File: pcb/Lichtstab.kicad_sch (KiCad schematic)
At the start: 0 parts

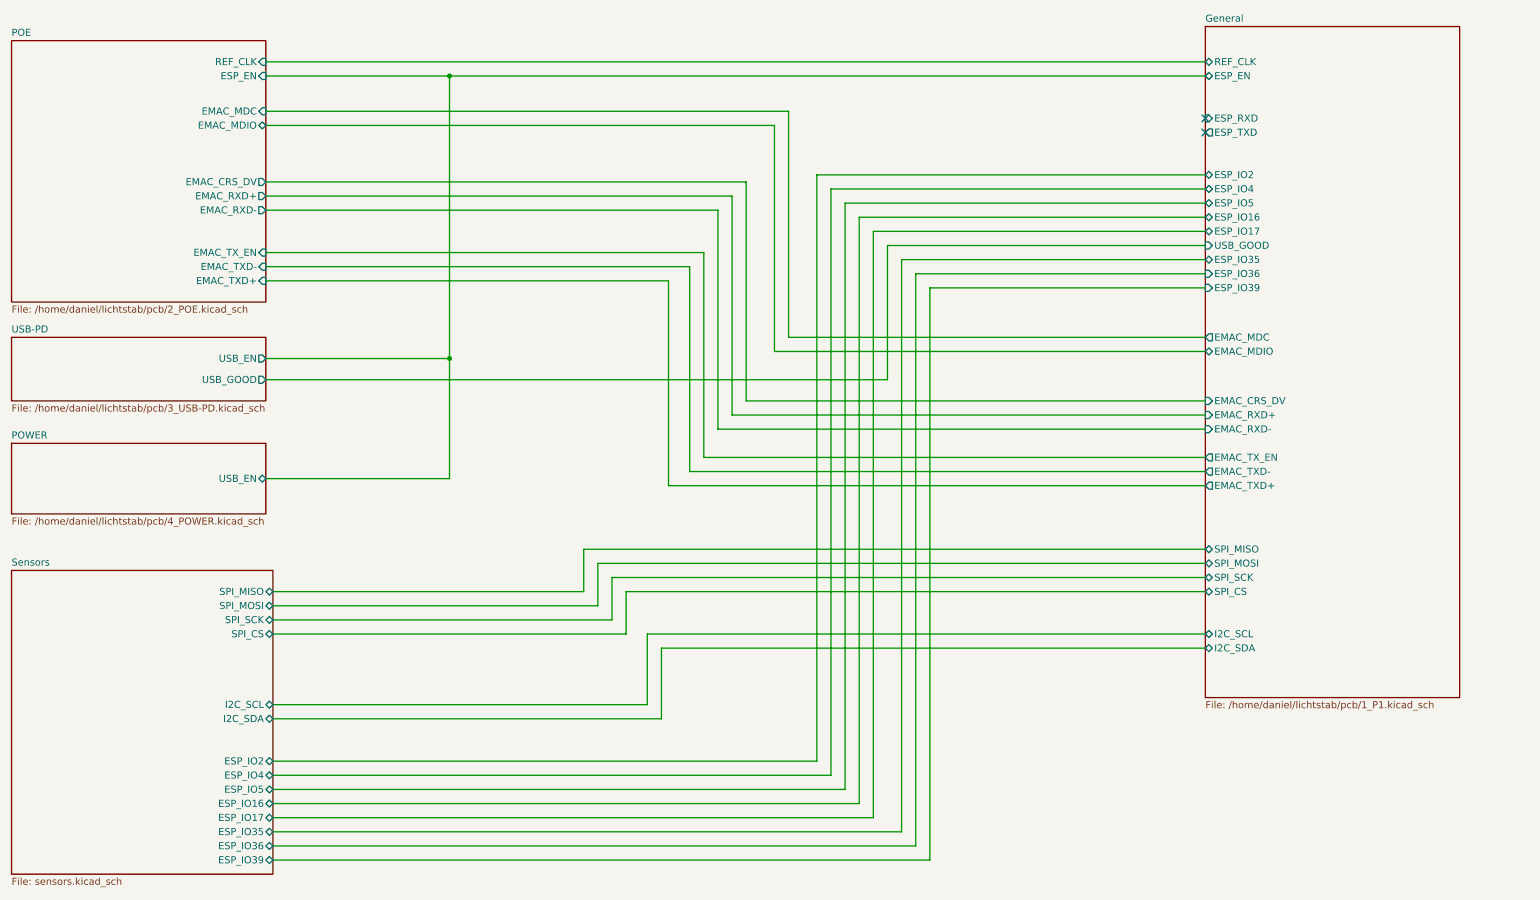
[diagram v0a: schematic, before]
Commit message: 4 layer pcb
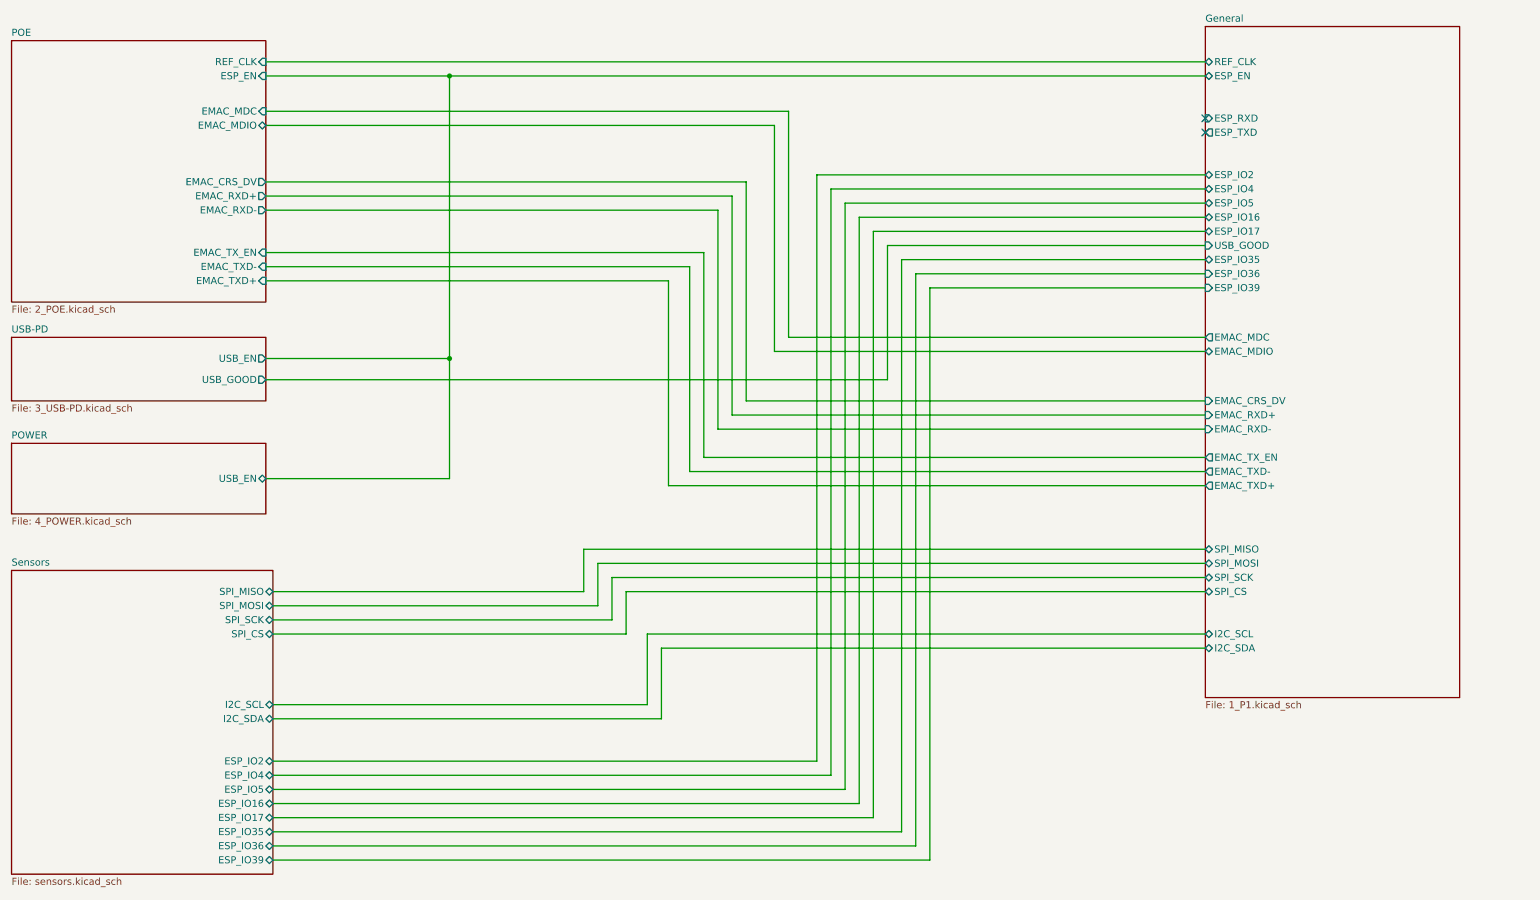
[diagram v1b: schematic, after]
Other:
- sheet General: file /home/daniel/lichtstab/pcb/1_P1.kicad_sch -> 1_P1.kicad_sch
- sheet POE: file /home/daniel/lichtstab/pcb/2_POE.kicad_sch -> 2_POE.kicad_sch
- sheet POWER: file /home/daniel/lichtstab/pcb/4_POWER.kicad_sch -> 4_POWER.kicad_sch
- sheet USB-PD: file /home/daniel/lichtstab/pcb/3_USB-PD.kicad_sch -> 3_USB-PD.kicad_sch
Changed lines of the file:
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@@
 			)
 		)
-		(property "Sheetfile" "/home/daniel/lichtstab/pcb/3_USB-PD.kicad_sch"
+		(property "Sheetfile" "3_USB-PD.kicad_sch"
 			(at 15.24 105.9946 0)
 			(effects
@@
 			)
 		)
-		(property "Sheetfile" "/home/daniel/lichtstab/pcb/4_POWER.kicad_sch"
+		(property "Sheetfile" "4_POWER.kicad_sch"
 			(at 15.24 126.3146 0)
 			(effects
@@
 			)
 		)
-		(property "Sheetfile" "/home/daniel/lichtstab/pcb/1_P1.kicad_sch"
+		(property "Sheetfile" "1_P1.kicad_sch"
 			(at 229.87 159.3346 0)
 			(effects
@@
 			)
 		)
-		(property "Sheetfile" "/home/daniel/lichtstab/pcb/2_POE.kicad_sch"
+		(property "Sheetfile" "2_POE.kicad_sch"
 			(at 15.24 88.2146 0)
 			(effects

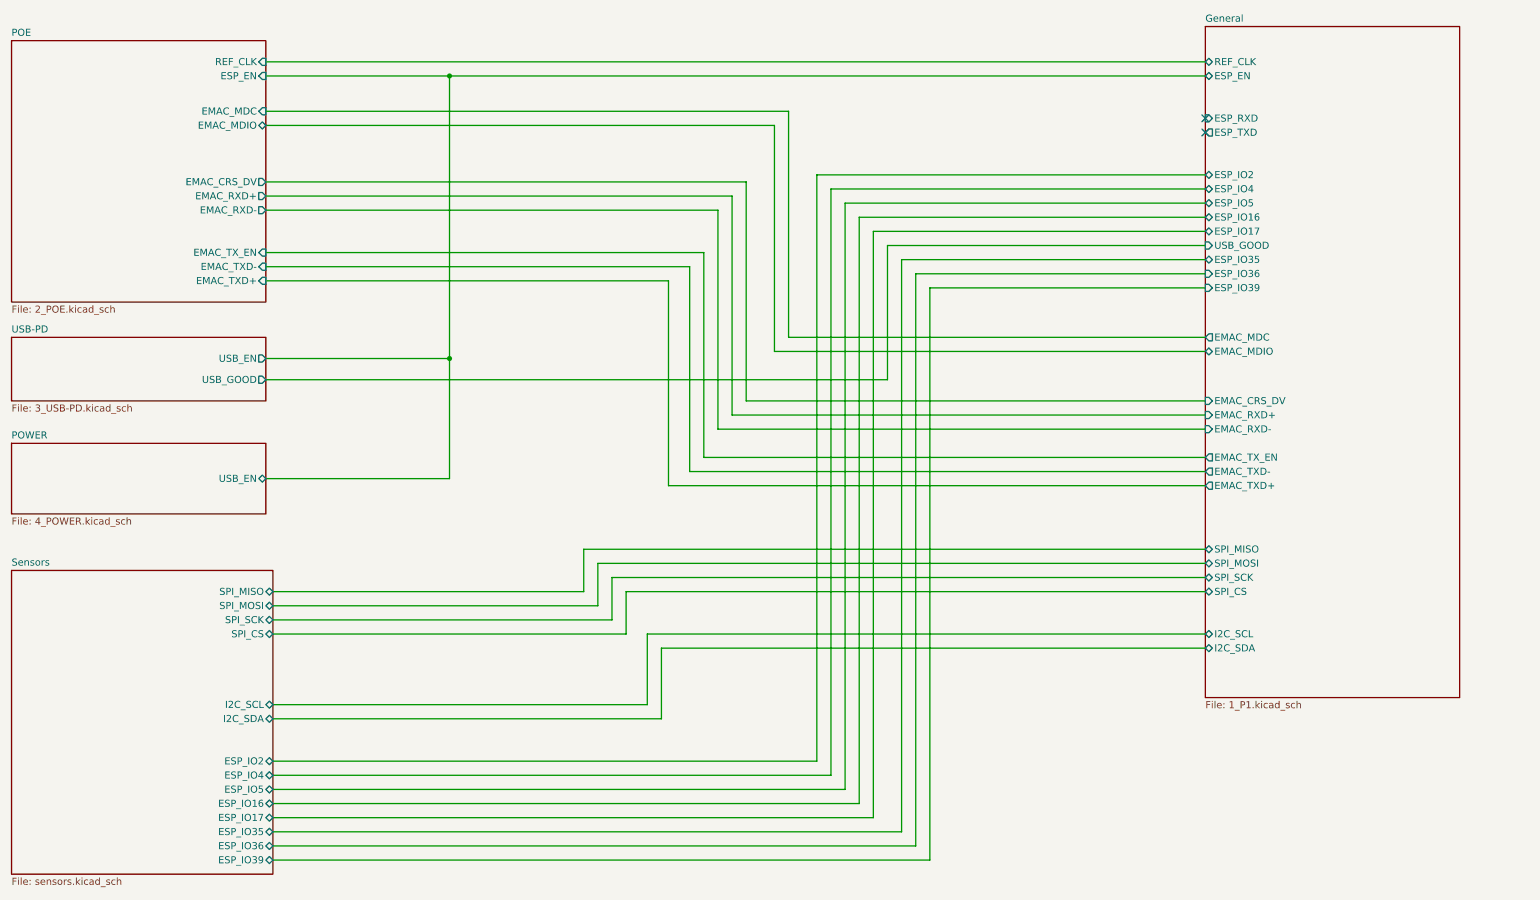
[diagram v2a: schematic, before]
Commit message: remove third pcb and more flash
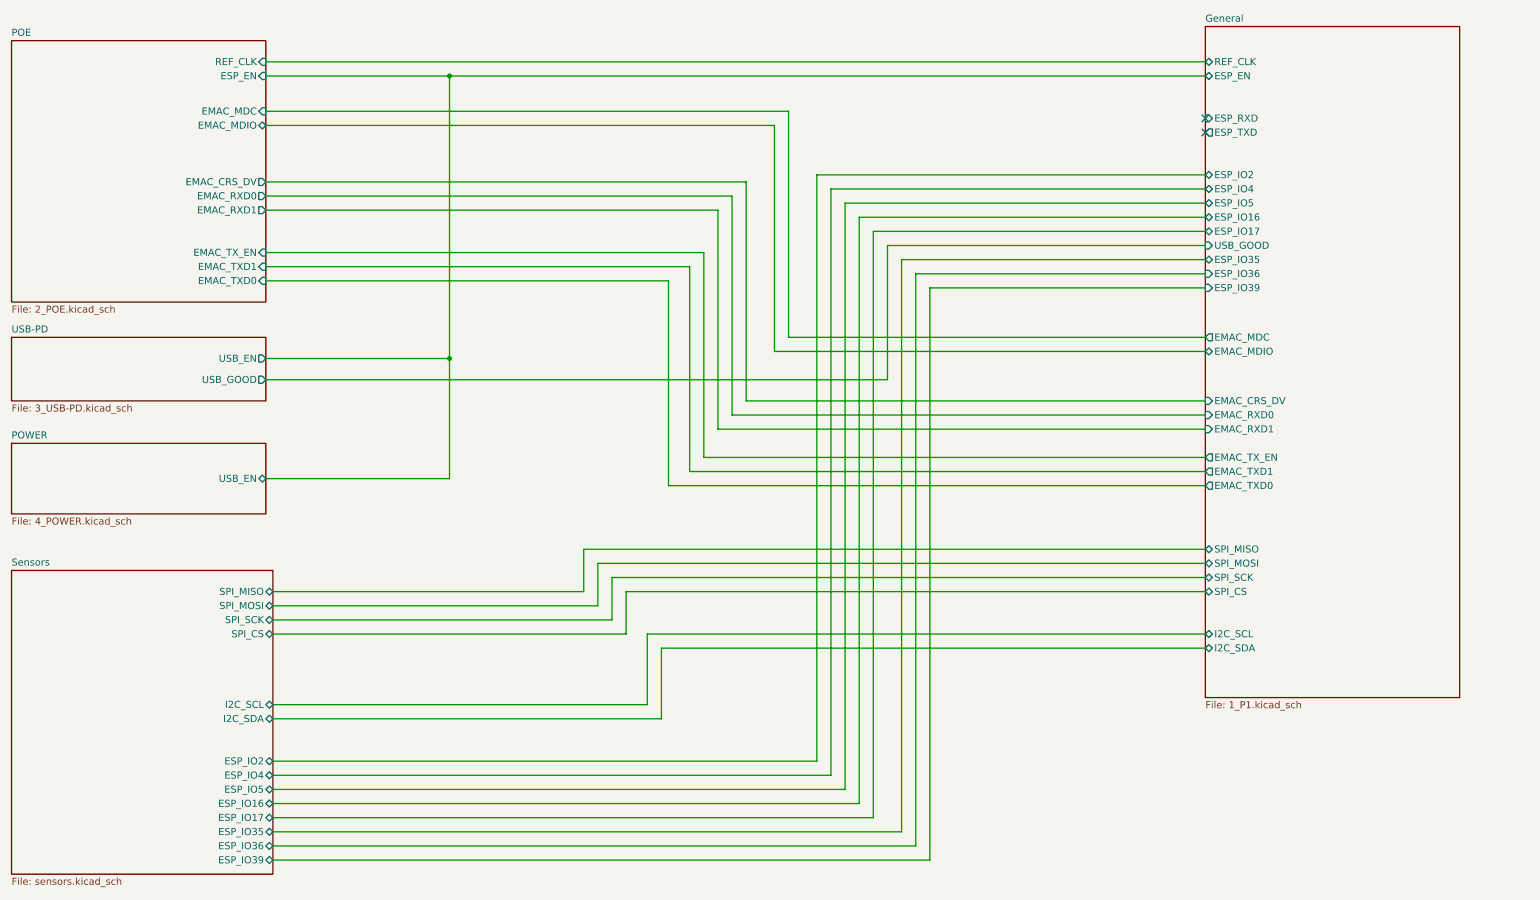
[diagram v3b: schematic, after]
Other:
- sheet General ports: added EMAC_RXD0, EMAC_RXD1, EMAC_TXD0, EMAC_TXD1; removed EMAC_RXD+, EMAC_RXD-, EMAC_TXD+, EMAC_TXD-
- sheet POE ports: added EMAC_RXD0, EMAC_RXD1, EMAC_TXD0, EMAC_TXD1; removed EMAC_RXD+, EMAC_RXD-, EMAC_TXD+, EMAC_TXD-
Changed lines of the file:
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@@
 			)
 		)
-		(pin "EMAC_TXD-" output
+		(pin "EMAC_TXD1" output
 			(at 229.87 118.11 180)
 			(effects
@@
 			)
 		)
-		(pin "EMAC_TXD+" output
+		(pin "EMAC_TXD0" output
 			(at 229.87 120.65 180)
 			(effects
@@
 			)
 		)
-		(pin "EMAC_RXD+" input
+		(pin "EMAC_RXD0" input
 			(at 229.87 107.95 180)
 			(effects
@@
 			)
 		)
-		(pin "EMAC_RXD-" input
+		(pin "EMAC_RXD1" input
 			(at 229.87 110.49 180)
 			(effects
@@
 			)
 		)
-		(pin "EMAC_TXD-" input
+		(pin "EMAC_TXD1" input
 			(at 60.96 81.28 0)
 			(effects
@@
 			)
 		)
-		(pin "EMAC_TXD+" input
+		(pin "EMAC_TXD0" input
 			(at 60.96 83.82 0)
 			(effects
@@
 			)
 		)
-		(pin "EMAC_RXD+" output
+		(pin "EMAC_RXD0" output
 			(at 60.96 68.58 0)
 			(effects
@@
 			)
 		)
-		(pin "EMAC_RXD-" output
+		(pin "EMAC_RXD1" output
 			(at 60.96 71.12 0)
 			(effects
